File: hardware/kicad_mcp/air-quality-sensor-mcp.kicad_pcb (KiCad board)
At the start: 2 copper layers, 80 x 60 mm, 16 parts, among them J1 JST_PH_2pin_Battery, U1 XIAO_ESP32C3, U2 Adafruit_SCD41, U3 Adafruit_SGP41, U4 SSD1306_OLED_128x64, U5 TP4056_USB-C_Module

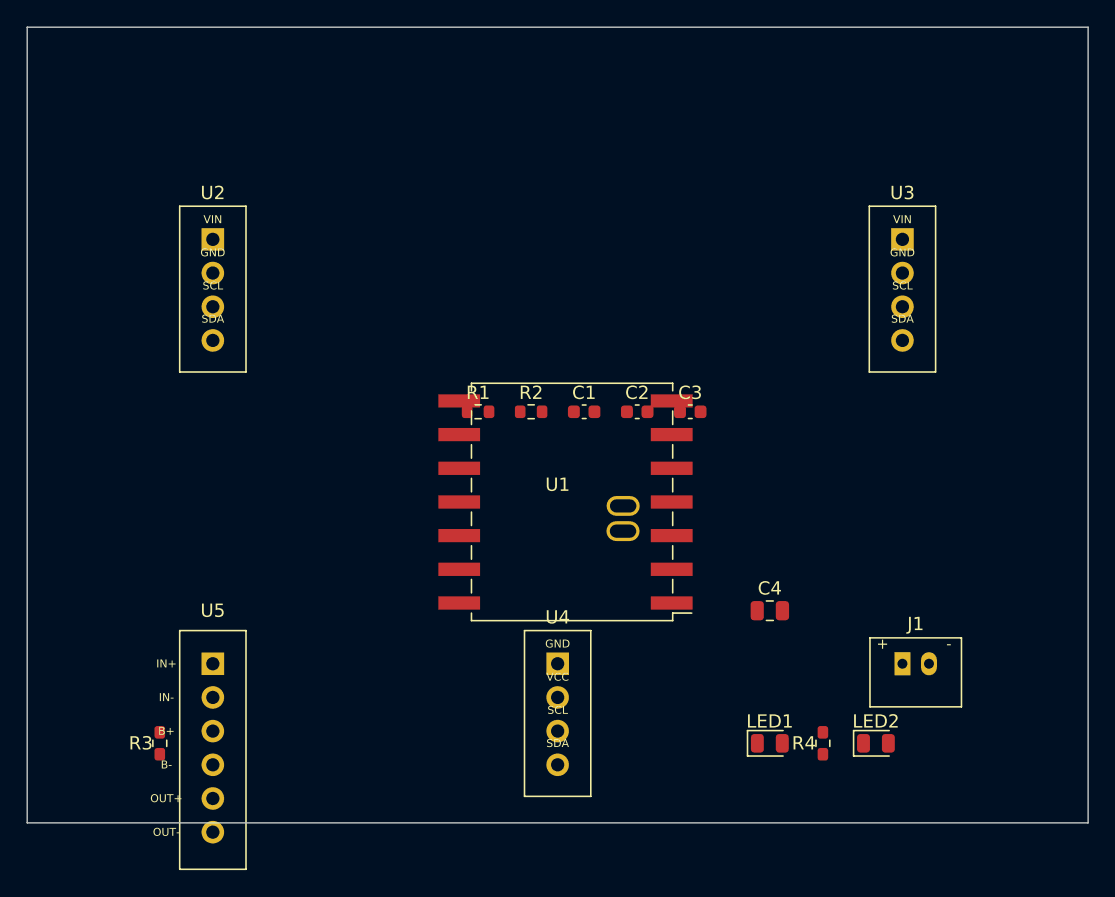
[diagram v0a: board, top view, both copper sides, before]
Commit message: Finalize MCP demo board, docs, and manufacturing outputs
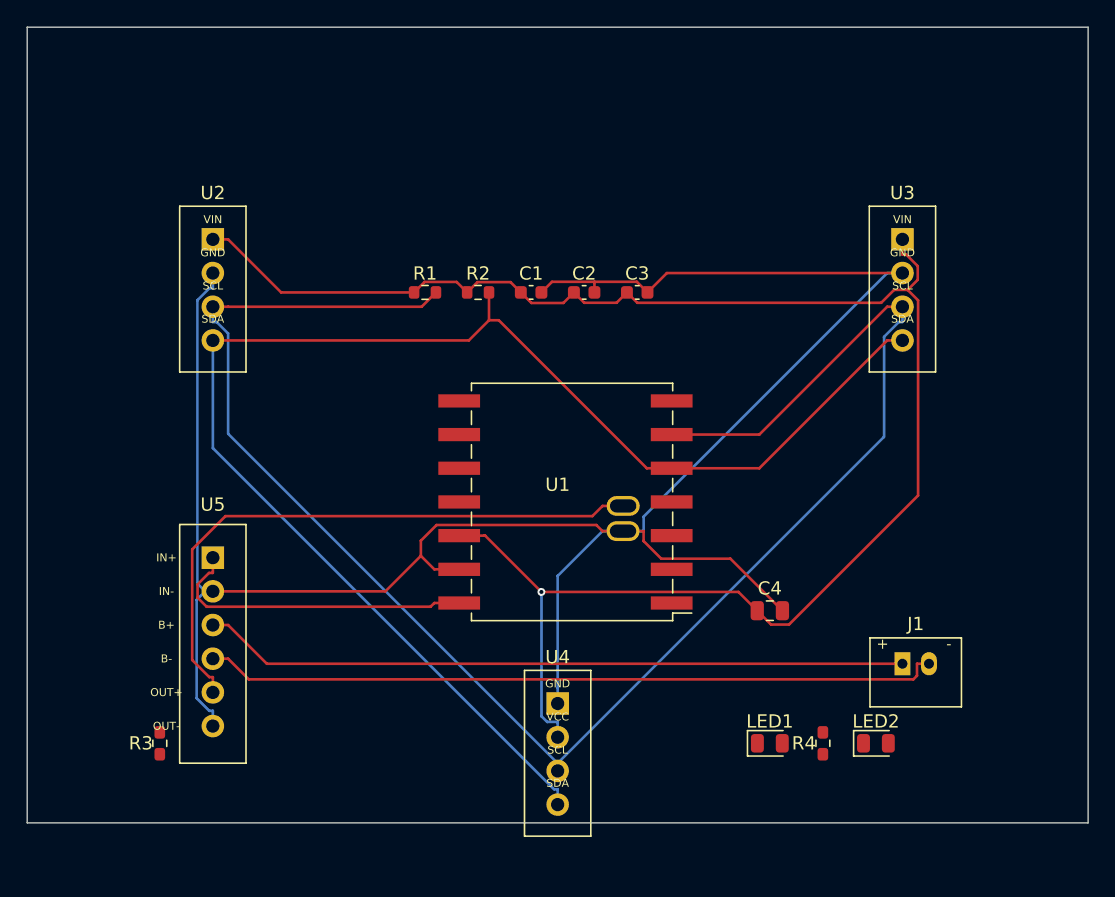
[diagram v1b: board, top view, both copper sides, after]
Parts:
- moved C1 9.85 mm to (48.0, 30.0)
- moved C2 9.85 mm to (52.0, 30.0)
- moved C3 9.85 mm to (56.0, 30.0)
- moved R1 9.85 mm to (40.0, 30.0)
- moved R2 9.85 mm to (44.0, 30.0)
- moved U5 8.00 mm to (24.0, 50.0)
- moved U4 3.00 mm to (50.0, 61.0)
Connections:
- C1 pad 1: (no net) -> +3V3
- C1 pad 2: (no net) -> GND
- C2 pad 1: (no net) -> +3V3
- C2 pad 2: (no net) -> GND
- C3 pad 1: (no net) -> +3V3
- C3 pad 2: (no net) -> GND
- C4 pad 1: (no net) -> +3V3
- C4 pad 2: (no net) -> GND
- J1 pad 1: (no net) -> BAT+
- J1 pad 2: (no net) -> BAT-
- LED1 pad 1: (no net) -> Net-(LED1-1)
- LED1 pad 2: (no net) -> Net-(LED1-2)
- LED2 pad 1: (no net) -> Net-(LED2-1)
- LED2 pad 2: (no net) -> Net-(LED2-2)
- R1 pad 1: (no net) -> +3V3
- R1 pad 2: (no net) -> I2C_SCL
- R2 pad 1: (no net) -> +3V3
- R2 pad 2: (no net) -> I2C_SDA
- R3 pad 1: (no net) -> Net-(R3-1)
- R3 pad 2: (no net) -> Net-(R3-2)
- R4 pad 1: (no net) -> Net-(R4-1)
- R4 pad 2: (no net) -> Net-(R4-2)
- U1 pad 1: (no net) -> Net-(U1-1)
- U1 pad 10: (no net) -> Net-(U1-10)
- U1 pad 11: (no net) -> Net-(U1-11)
- U1 pad 12: (no net) -> +3V3
- U1 pad 13: (no net) -> GND
- U1 pad 14: (no net) -> USB_5V
- U1 pad 2: (no net) -> Net-(U1-2)
- U1 pad 3: (no net) -> Net-(U1-3)
- U1 pad 4: (no net) -> Net-(U1-4)
- U1 pad 5: (no net) -> I2C_SDA
- U1 pad 6: (no net) -> I2C_SCL
- U1 pad 7: (no net) -> Net-(U1-7)
- U1 pad 8: (no net) -> Net-(U1-8)
- U1 pad 9: (no net) -> Net-(U1-9)
- U1 pad B+: (no net) -> VBAT
- U1 pad B-: (no net) -> GND
- U2 pad 1: (no net) -> +3V3
- U2 pad 2: (no net) -> GND
- U2 pad 3: (no net) -> I2C_SCL
- U2 pad 4: (no net) -> I2C_SDA
- U3 pad 1: (no net) -> +3V3
- U3 pad 2: (no net) -> GND
- U3 pad 3: (no net) -> I2C_SCL
- U3 pad 4: (no net) -> I2C_SDA
- U4 pad 1: (no net) -> GND
- U4 pad 2: (no net) -> +3V3
- U4 pad 3: (no net) -> I2C_SCL
- U4 pad 4: (no net) -> I2C_SDA
- U5 pad 1: (no net) -> USB_5V
- U5 pad 2: (no net) -> GND
- U5 pad 3: (no net) -> BAT+
- U5 pad 4: (no net) -> BAT-
- U5 pad 5: (no net) -> VBAT
- U5 pad 6: (no net) -> GND
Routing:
- net GND: track 0.00 -> 163.7 mm
- net +3V3: track 0.00 -> 131.3 mm, vias 0 -> 1
- net I2C_SCL: track 0.00 -> 130.0 mm
- net I2C_SDA: track 0.00 -> 109.3 mm
- net BAT-: track 0.00 -> 55.7 mm
- net BAT+: track 0.00 -> 53.2 mm
- net VBAT: track 0.00 -> 45.4 mm
- net USB_5V: track 0.00 -> 23.8 mm
